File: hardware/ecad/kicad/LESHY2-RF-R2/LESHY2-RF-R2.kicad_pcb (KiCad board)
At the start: 6 copper layers, 80 x 150 mm, 784 parts, among them J1 JAE DX07S016JA1R1500, J10 Samtec HLE-107-02-G-DV-PE-LC, J11 1125R-SMT-4P, J12 Hirose FX8C-80S-SV5(92), J13 Samtec FTSH-105-01-L-DV-K-P-TR, J2 Samtec FTSH-105-01-L-DV-K-P-TR, J3 Samtec FTSH-105-01-L-DV-K-P-TR, J4 GCT USB4105-GF-A, J5 GCT RFPC-SMA31-FN-175-A, J6 GCT RFPC-SMA31-FN-175-A, J7 GCT RFPC-SMA31-FN-175-A, J8 GCT RFPC-SMA31-FN-175-A, J9 GCT RFPC-SMA31-FN-175-A, Q1 Diodes Incorporated DMN2056U-7, Q2 Diodes Incorporated 2N7002DW-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, Q3 Diodes Incorporated 2N7002DW-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, Q4 Diodes Incorporated MMBT3904-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, Q5 Diodes Incorporated MMBT3904-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, Q6 Diodes Incorporated 2N7002DW-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, SW1 Alps Alpine SKRTLAE010, SW2 Alps Alpine SKRTLAE010, SW3 Alps Alpine EC11E18244AU, SW4 OMRON B3S-1100P, SW5 C&K JS102011SAQN, U1 Texas Instruments BQ25798RQMR, U10 Texas Instruments CSD87313DMS, U100 Texas Instruments TPS259470LR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, U101 Texas Instruments TPD4E05U06D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, U102 Texas Instruments TXS0102DCUR, U103 TPS3808G33DBVR, U104 Texas Instruments TPD4E05U06D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, U105 Texas Instruments TPD4E05U06D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, U106 TCA6424ARGJR, U107 Diodes Incorporated BAT54-7-F, U108 TLV1821DCKR, U109 TLV1821DCKR, U11 onsemi BAV70LT1G, U110 TLV1821DCKR, U111 TCA9535PWR, U112 BAT54ALT1G, U113 BAT54ALT1G, U114 BAT54ALT1G, U115 BAT54ALT1G, U116 BAT54ALT1G, U117 74LVC2G14GV,125, U118 SN74LVC3G07DCUR, U119 SN74LVC08APWR, U12 Diodes Incorporated BAT54-7-F, U120 SN74LVC1G74DCUR, U121 74LVC1G32GV,125, U122 SN74LVC1G17DCKR, U123 Texas Instruments SN74LVC1G06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, U124 SN74LVC1G07DCKR, U125 TPS3808G33DBVR, U126 Texas Instruments TPD4E05U06D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, U127 Texas Instruments MSPM0C1106S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, U128 SN74LVC1G07DCKR, U129 SN74LVC1G07DCKR, U13 Texas Instruments TPS629203DR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, U130 Texas Instruments TPS3435CAKA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, U131 SN74LVC1G07DCKR, U132 SN74LVC1G07DCKR, U133 Diodes Incorporated BAT54-7-F, U134 Diodes Incorporated BAT54-7-F, U14 Texas Instruments TPS25961DRVR, U15 Texas Instruments SN74LVC2G08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, U16 Texas Instruments TPS564252DR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, U17 Texas Instruments TPS259470LR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, U18 SN74LVC1G07DCKR, U19 74LVC1G32GV,125, U2 onsemi CAT24C512WI-GT3, U20 TPS566231PRQFR, U21 Texas Instruments TPS25974LRP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, U22 PSPMAA0605H-2R2M-ANP, U23 SC1512-A4, U24 Texas Instruments TPD4E05U06D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, U25 Texas Instruments TPD2EUSB30A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, U26 onsemi FSUSB42MUX, U27 CC1101RGPR, U28 SN74LVC1G08DCKR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

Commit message: Widen antenna spacing and recess microSD with exact native guards
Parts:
- moved U33 9.00 mm to (62.0, 3.95), turned to 90 degrees
- moved J7 5.90 mm to (69.4, 0.00)
- moved J9 5.90 mm to (10.6, 0.00)
- moved C126 4.33 mm to (66.7, 4.10)
- moved J6 2.95 mm to (54.7, 0.00)
- moved J8 2.95 mm to (25.3, 0.00)
- moved C182 2.35 mm to (29.7, 3.29)
- moved C180 1.75 mm to (25.3, 1.60)
- moved C161 1.67 mm to (10.7, 1.10)
- moved D4 1.50 mm to (29.8, 0.86)
- moved C169 1.45 mm to (25.3, 3.31)
- moved C162 1.17 mm to (10.7, 2.60)
- moved C170 1.00 mm to (20.3, 2.60)
- moved C173 0.30 mm to (20.8, 1.35)
- moved C163 0.14 mm to (11.1, 3.75)
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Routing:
- net /RF_21_BROADCAST_AIRBAND_RX/RX_AMLW_BOUNDARY_RF: track 6.39 -> 10.2 mm
- net /RF_21_BROADCAST_AIRBAND_RX/AIR_BPF_OUT_RF: track 7.74 -> 4.45 mm
- net /RF_21_BROADCAST_AIRBAND_RX/AIR_LO_PAD: track 7.88 -> 6.54 mm

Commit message: Correct EC11 fit and add seven reviewed LED routes
Integrate the exact-axis engineering EC11 footprint and local support placement while preserving all765 RF copper objects and five encoder world pad/net pairs. Add51 UI segments and8 vias for seven reviewed anode nets, retaining all33 prior UI copper objects and excluding FAULT.

Refresh native DRC, four-face component views, routing counters, H3 contract hashes, typed ERC and source-path triage. Correct stale holder/JAE evidence wording; retain24 raw ERC findings, open mechanical/power gates and historical firmware qualification. Add actual-files freshness and public-counter regressions.

Checks:1182 hardware tests with46 skips;116 native focused tests without skips; both boards DRC0 violations/0 schematic-parity findings;115 routes,682 segments,175 vias,197 resolved,3071 remaining. No new MPN, order or fabrication authorization.
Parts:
- SW3: footprint Rotary_Encoder:RotaryEncoder_Alps_EC11E-Switch_Vertical_H20mm_MountingHoles -> Leshy2_R2:EC11E18244AU-ENGINEERING-PTH
- moved C153 14.5 mm to (66.8, 47.9), turned to 90 degrees
- moved U134 10.0 mm to (77.5, 54.7)
- moved SW3 7.91 mm to (71.0, 50.2), turned to 0 degrees
- moved C152 7.54 mm to (71.7, 45.4), turned to 90 degrees
- moved R111 6.20 mm to (58.8, 52.2)
- moved C240 6.19 mm to (61.6, 52.2)
- moved C288 4.23 mm to (71.9, 48.0), turned to 90 degrees
- moved R221 4.08 mm to (71.5, 54.3)
- moved R180 3.69 mm to (71.0, 55.9), turned to 180 degrees
- moved U38 3.49 mm to (69.2, 47.9), turned to 90 degrees
- moved R209 2.86 mm to (67.8, 56.1)
- moved R112 2.60 mm to (66.4, 58.4)
- moved R143 1.72 mm to (69.1, 52.2), turned to 90 degrees
- moved R104 0.98 mm to (62.7, 50.5)
- moved U90 0.80 mm to (61.5, 55.6)
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
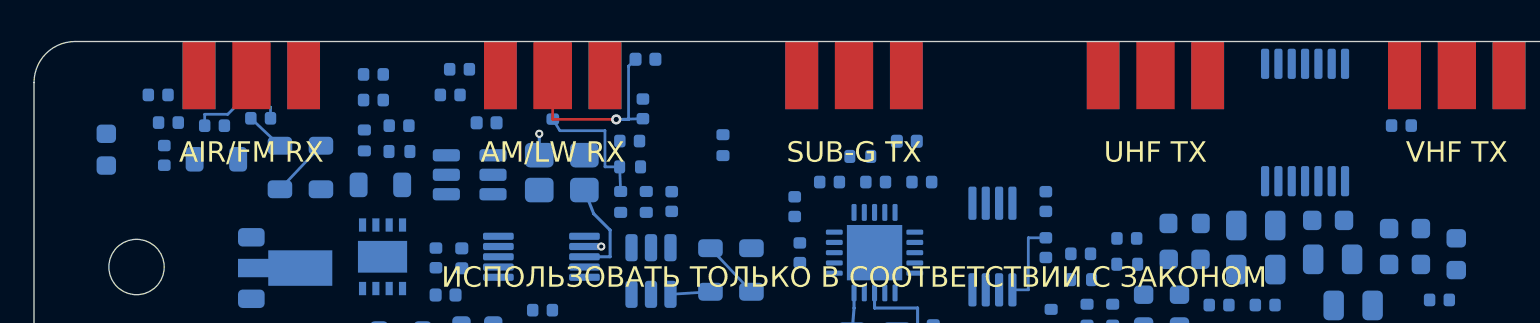
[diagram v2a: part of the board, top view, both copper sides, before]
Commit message: Clear SMA solder access with bounded support relocations
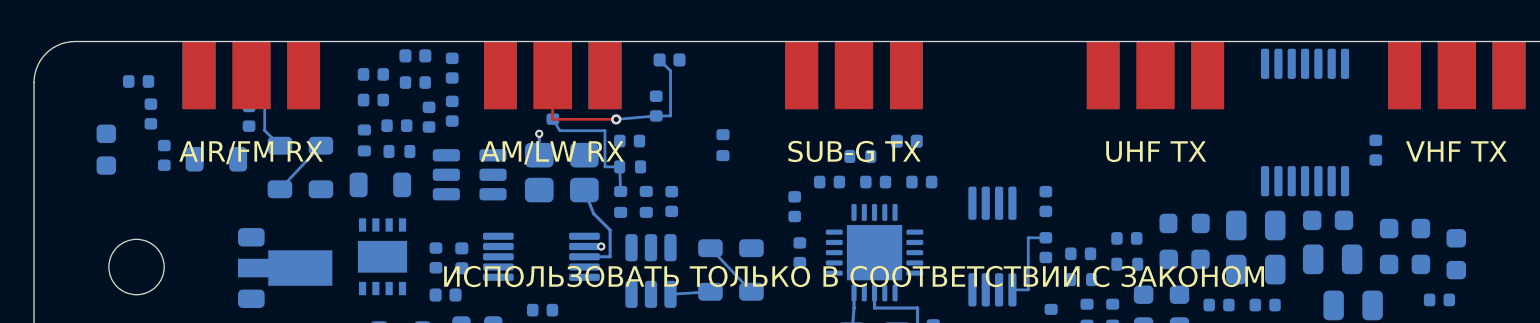
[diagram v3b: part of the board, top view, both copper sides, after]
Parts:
- moved C161 8.95 mm to (19.3, 3.69), turned to 90 degrees
- moved C162 7.92 mm to (18.6, 2.00)
- moved D5 4.77 mm to (18.6, 0.70)
- moved C163 2.51 mm to (10.5, 1.30), turned to 90 degrees
- moved C165 1.75 mm to (10.5, 3.65), turned to -90 degrees
- moved C126 1.73 mm to (65.5, 5.30), turned to -90 degrees
- moved D4 1.18 mm to (31.0, 0.90)
- moved C166 1.16 mm to (5.10, 1.95)
- moved C167 0.95 mm to (5.70, 3.54), turned to 90 degrees
- moved C170 0.80 mm to (20.4, 3.40), turned to 90 degrees
- moved C182 0.66 mm to (30.4, 3.15)
- moved C180 0.41 mm to (25.3, 1.20), turned to 90 degrees
- moved C173 0.36 mm to (20.4, 1.30), turned to 90 degrees
- moved C158 0.11 mm to (17.7, 4.11)
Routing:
- net /RF_21_BROADCAST_AIRBAND_RX/AIR_BPF_S3_LC: track 1.95 -> 3.92 mm
- net /RF_21_BROADCAST_AIRBAND_RX/AIR_BPF_OUT_RF: track 4.45 -> 3.49 mm
- net /RF_21_BROADCAST_AIRBAND_RX/RX_AMLW_BOUNDARY_RF: track 10.2 -> 10.9 mm
